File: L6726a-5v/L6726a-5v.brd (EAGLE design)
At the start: 80.3 x 19 mm, 28 parts, among them IC1 L6726A, IC2 MCP1804

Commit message: a few more tweaks!
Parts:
- IC2: value MCP1804 -> (none)
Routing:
- net VCC: track 21.8 -> 20.6 mm
- net GND: vias 146 -> 151
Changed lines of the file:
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@@
 <layer number="17" name="Pads" color="2" fill="1" visible="yes" active="yes"/>
 <layer number="18" name="Vias" color="2" fill="1" visible="yes" active="yes"/>
-<layer number="19" name="Unrouted" color="6" fill="1" visible="yes" active="yes"/>
+<layer number="19" name="Unrouted" color="14" fill="1" visible="yes" active="yes"/>
 <layer number="20" name="Dimension" color="15" fill="1" visible="yes" active="yes"/>
 <layer number="21" name="tPlace" color="7" fill="1" visible="yes" active="yes"/>
@@
 </element>
 <element name="CHF" library="rcl" package="C1206" value="10u" x="37.7825" y="9.525" smashed="yes">
-<attribute name="NAME" x="34.925" y="8.89" size="0.6096" layer="25" font="vector" ratio="14" rot="R90"/>
+<attribute name="NAME" x="38.735" y="11.1125" size="0.6096" layer="25" font="vector" ratio="14" rot="R180"/>
 </element>
 <element name="COUT1" library="rcl" package="SANYO-OSCON_SMD_C6" value="330u" x="67.945" y="13.97" smashed="yes" rot="R180">
@@
 </element>
 <element name="CBULK1" library="rcl" package="C2220K" value="33u" x="20.955" y="12.7" smashed="yes" rot="R90">
-<attribute name="NAME" x="17.37" y="11.17" size="0.6096" layer="25" font="vector" ratio="14" rot="R90"/>
+<attribute name="NAME" x="22.8025" y="13.2425" size="0.6096" layer="25" font="vector" ratio="14" rot="R180"/>
 </element>
 <element name="CBULK2" library="rcl" package="C2220K" value="33u" x="20.955" y="5.08" smashed="yes" rot="R270">
-<attribute name="NAME" x="17.37" y="4.185" size="0.6096" layer="25" font="vector" ratio="14" rot="R90"/>
+<attribute name="NAME" x="22.8025" y="5.6225" size="0.6096" layer="25" font="vector" ratio="14" rot="R180"/>
 </element>
 <element name="CBULK3" library="rcl" package="C2220K" value="33u" x="29.21" y="5.08" smashed="yes" rot="R270">
-<attribute name="NAME" x="25.625" y="4.185" size="0.6096" layer="25" font="vector" ratio="14" rot="R90"/>
+<attribute name="NAME" x="31.0575" y="5.6225" size="0.6096" layer="25" font="vector" ratio="14" rot="R180"/>
 </element>
 <element name="CBULK4" library="rcl" package="C2220K" value="33u" x="29.21" y="12.7" smashed="yes" rot="R90">
-<attribute name="NAME" x="25.9425" y="11.17" size="0.6096" layer="25" font="vector" ratio="14" rot="R90"/>
+<attribute name="NAME" x="31.0575" y="13.2425" size="0.6096" layer="25" font="vector" ratio="14" rot="R180"/>
 </element>
 <element name="LS" library="SparkFun-DiscreteSemi" package="SO08" value="" x="43.4975" y="5.715" smashed="yes" rot="R270">
@@
 <attribute name="VALUE" x="46.815" y="10.6525" size="1.016" layer="27" font="vector" ratio="15" rot="R180"/>
 </element>
-<element name="IC2" library="microchip-vreg" package="SOT23-5" value="MCP1804" x="21.2725" y="9.525" smashed="yes" rot="MR270">
+<element name="IC2" library="microchip-vreg" package="SOT23-5" value="" x="21.2725" y="9.525" smashed="yes" rot="MR270">
 <attribute name="NAME" x="19.1135" y="11.303" size="0.6096" layer="26" font="vector" ratio="14" rot="MR270"/>
 <attribute name="VALUE" x="19.4945" y="12.0015" size="0.6096" layer="28" font="vector" ratio="14" rot="MR180"/>
@@
 <signals>
 <signal name="VCC">
-<contactref element="CDEC" pad="1"/>
-<contactref element="IC1" pad="5"/>
-<contactref element="RD" pad="1"/>
-<wire x1="33.655" y1="8.89" x2="33.655" y2="8.95" width="0.4064" layer="16"/>
-<wire x1="33.655" y1="8.04" x2="33.655" y2="8.89" width="0.3048" layer="16"/>
-<wire x1="31.115" y1="7.2" x2="31.115" y2="8.255" width="0.3048" layer="16"/>
-<wire x1="31.115" y1="8.255" x2="31.75" y2="8.89" width="0.3048" layer="16" curve="-90"/>
-<wire x1="31.75" y1="8.89" x2="33.655" y2="8.89" width="0.3048" layer="16"/>
-<wire x1="29.21" y1="7.2" x2="31.115" y2="7.2" width="0.4064" layer="16"/>
 <contactref element="IC2" pad="5"/>
 <contactref element="CVROUT" pad="1"/>
@@
 <wire x1="20.0025" y1="7.3025" x2="18.7325" y2="8.5725" width="0.3048" layer="16" curve="-90"/>
 <wire x1="18.7325" y1="8.5725" x2="18.7325" y2="10.375" width="0.3048" layer="16"/>
+<contactref element="IC1" pad="5"/>
+<contactref element="RD" pad="1"/>
+<contactref element="CDEC" pad="1"/>
+<wire x1="33.655" y1="8.95" x2="32.386415625" y2="8.95" width="0.3048" layer="16"/>
+<wire x1="32.386415625" y1="8.95" x2="31.115" y2="7.678584375" width="0.3048" layer="16" curve="90"/>
+<wire x1="31.115" y1="7.678584375" x2="31.115" y2="7.2" width="0.3048" layer="16"/>
 <wire x1="29.21" y1="7.3025" x2="29.21" y2="7.2" width="0.3048" layer="16"/>
+<wire x1="29.21" y1="7.2" x2="31.115" y2="7.2" width="0.3048" layer="16"/>
 </signal>
 <signal name="+12V">
@@
 <wire x1="23.63730625" y1="9.525" x2="24.111359375" y2="9.328640625" width="0.3048" layer="16" curve="-45.000189"/>
 <wire x1="24.111359375" y1="9.328640625" x2="24.765" y2="8.675" width="0.3048" layer="16"/>
-<wire x1="30.1625" y1="10.58" x2="30.1625" y2="8.5725" width="0.254" layer="16"/>
 <via x="74.295" y="17.145" extent="1-16" drill="0.5"/>
 <via x="75.565" y="17.145" extent="1-16" drill="0.5"/>
@@
 <via x="58.7375" y="1.5875" extent="1-16" drill="0.381"/>
 <via x="59.69" y="1.5875" extent="1-16" drill="0.381"/>
+<wire x1="30.1625" y1="10.58" x2="30.1625" y2="8.5725" width="0.3048" layer="16"/>
+<via x="24.4475" y="4.7625" extent="1-16" drill="0.381"/>
+<via x="25.7175" y="4.7625" extent="1-16" drill="0.381"/>
+<via x="42.545" y="4.3815" extent="1-16" drill="0.3048"/>
+<via x="43.815" y="3.7465" extent="1-16" drill="0.3048"/>
+<via x="44.45" y="7.239" extent="1-16" drill="0.3048"/>
 </signal>
 <signal name="BOOT">
@@
 <vertex x="56.515" y="15.80005" curve="-90"/>
 <vertex x="57.22495" y="16.51"/>
-<vertex x="67.945" y="16.51"/>
+<vertex x="67.31" y="16.51" curve="-90"/>
+<vertex x="67.945" y="15.875"/>
 <vertex x="67.945" y="3.56745" curve="-90"/>
 </polygon>
@@
 <vertex x="53.6575" y="3.56745" curve="-90"/>
 <vertex x="52.94755" y="2.8575"/>
-<vertex x="45.72" y="2.8575"/>
+<vertex x="46.0375" y="2.8575" curve="-90"/>
+<vertex x="45.72" y="3.175"/>
 </polygon>
 <via x="52.705" y="5.08" extent="1-16" drill="0.3048"/>
@@
 <vertex x="47.9425" y="8.1234875" curve="90"/>
 <vertex x="47.4934875" y="8.5725"/>
-<vertex x="42.545" y="8.5725" curve="90"/>
-<vertex x="41.91" y="7.9375"/>
-<vertex x="41.91" y="2.8575"/>
+<vertex x="45.8515125" y="8.5725" curve="90"/>
+<vertex x="45.4025" y="8.1234875"/>
+<vertex x="45.4025" y="3.3065125" curve="90"/>
+<vertex x="45.8515125" y="2.8575"/>
 </polygon>
 <via x="46.6725" y="10.4775" extent="1-16" drill="0.3048"/>

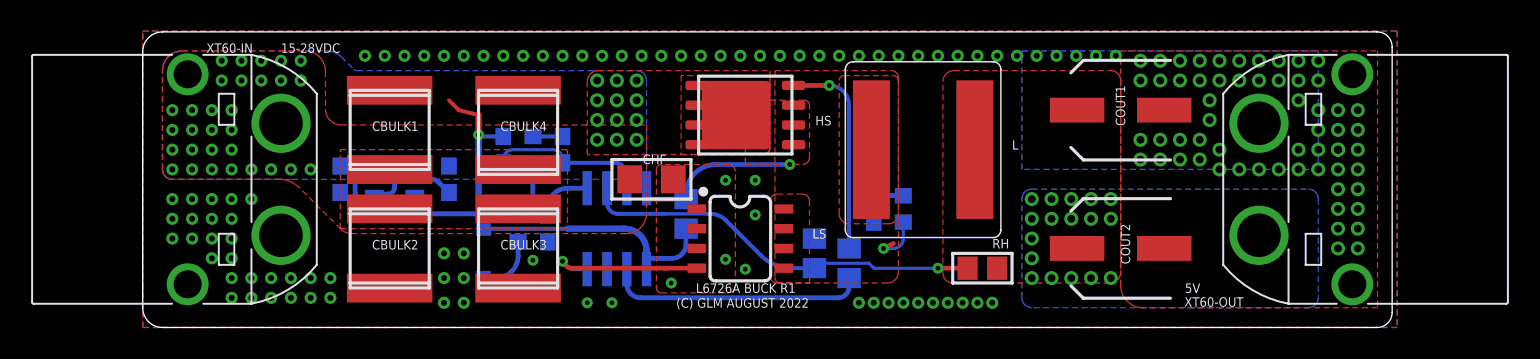
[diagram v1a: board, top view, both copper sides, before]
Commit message: updated DRU rules from Osh Park, finale tweaks to layout
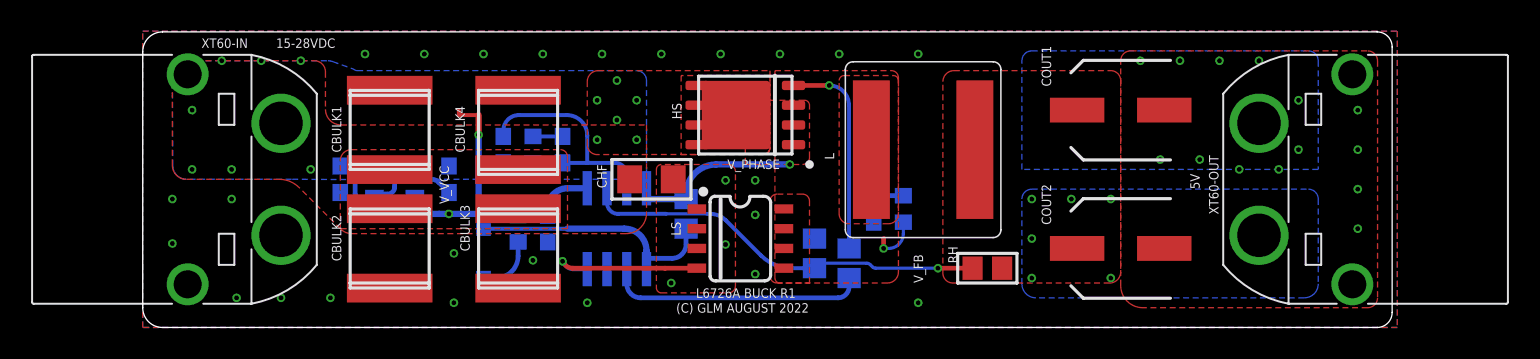
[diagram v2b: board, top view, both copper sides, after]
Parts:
- moved RH 0.32 mm to (59.4, 3.81)
- turned CP to 270 degrees
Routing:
- net COMP: track 10.1 -> 14.0 mm
- net GND: track 13.5 -> 12.8 mm, vias 151 -> 42
- net VCC: vias 0 -> 1
- net +12V: vias 42 -> 13
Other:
- board text added: "HS_GATE"
- board text added: "LS_GATE"
- board text added: "V_FB"
- board text added: "V_PHASE"
- board text added: "V_VCC"
